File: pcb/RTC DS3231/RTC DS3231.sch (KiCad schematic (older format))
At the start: 19 parts, among them J101 Conn_01x06_Male, J102 Conn_01x04_Male, U101 DS3231M, U102 AT24CS32-SSHM

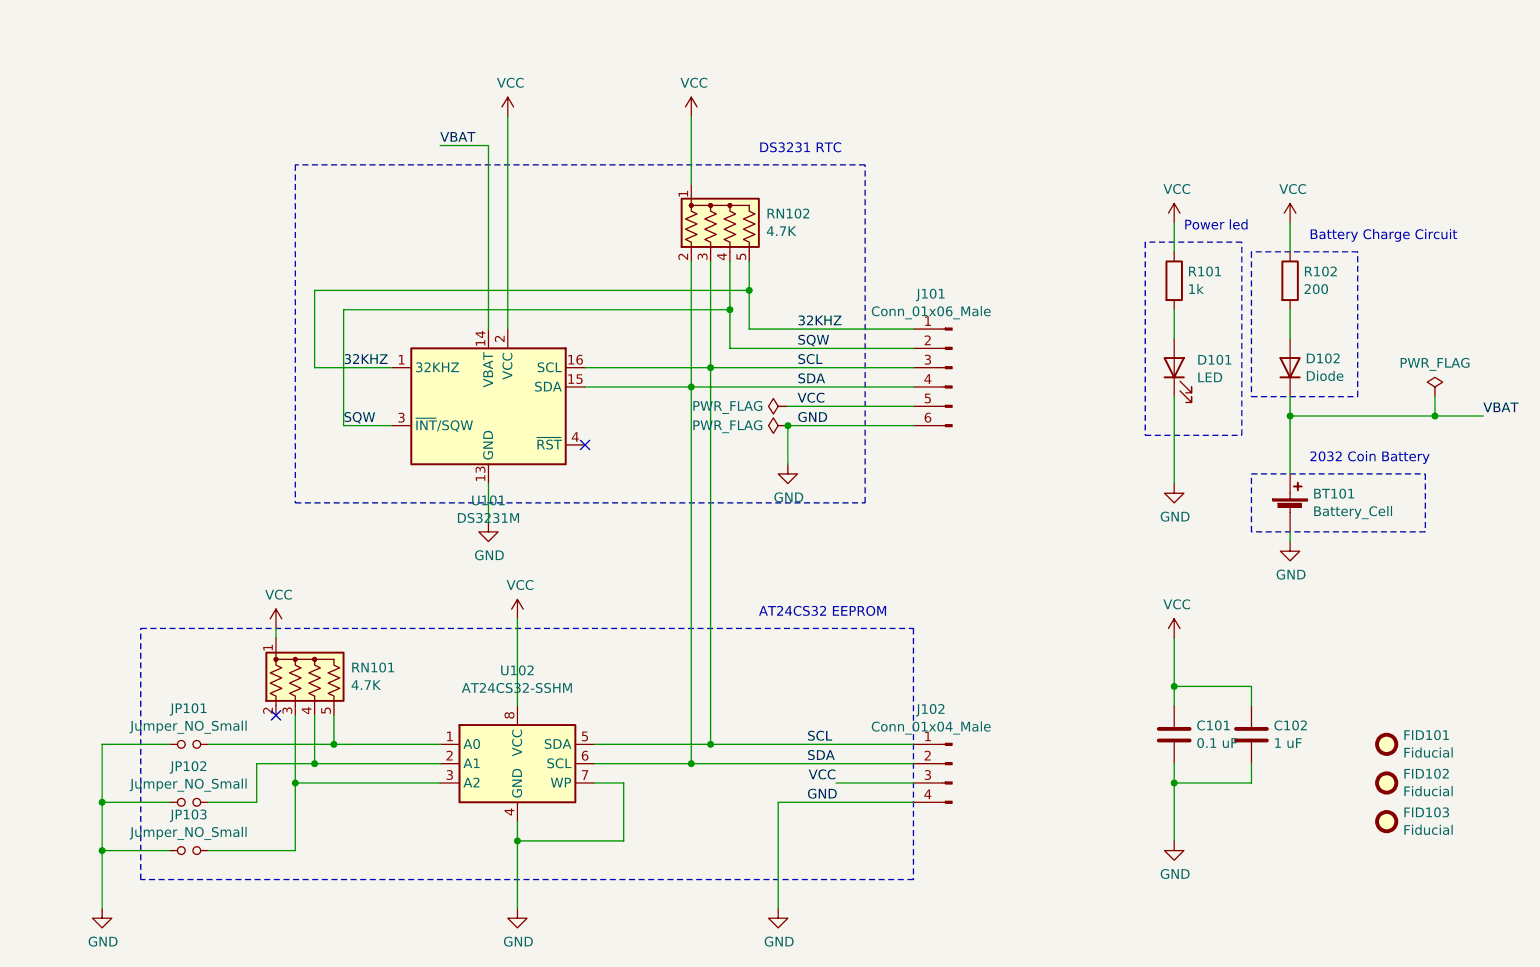
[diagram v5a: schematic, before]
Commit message: Update RTC DS3231.sch
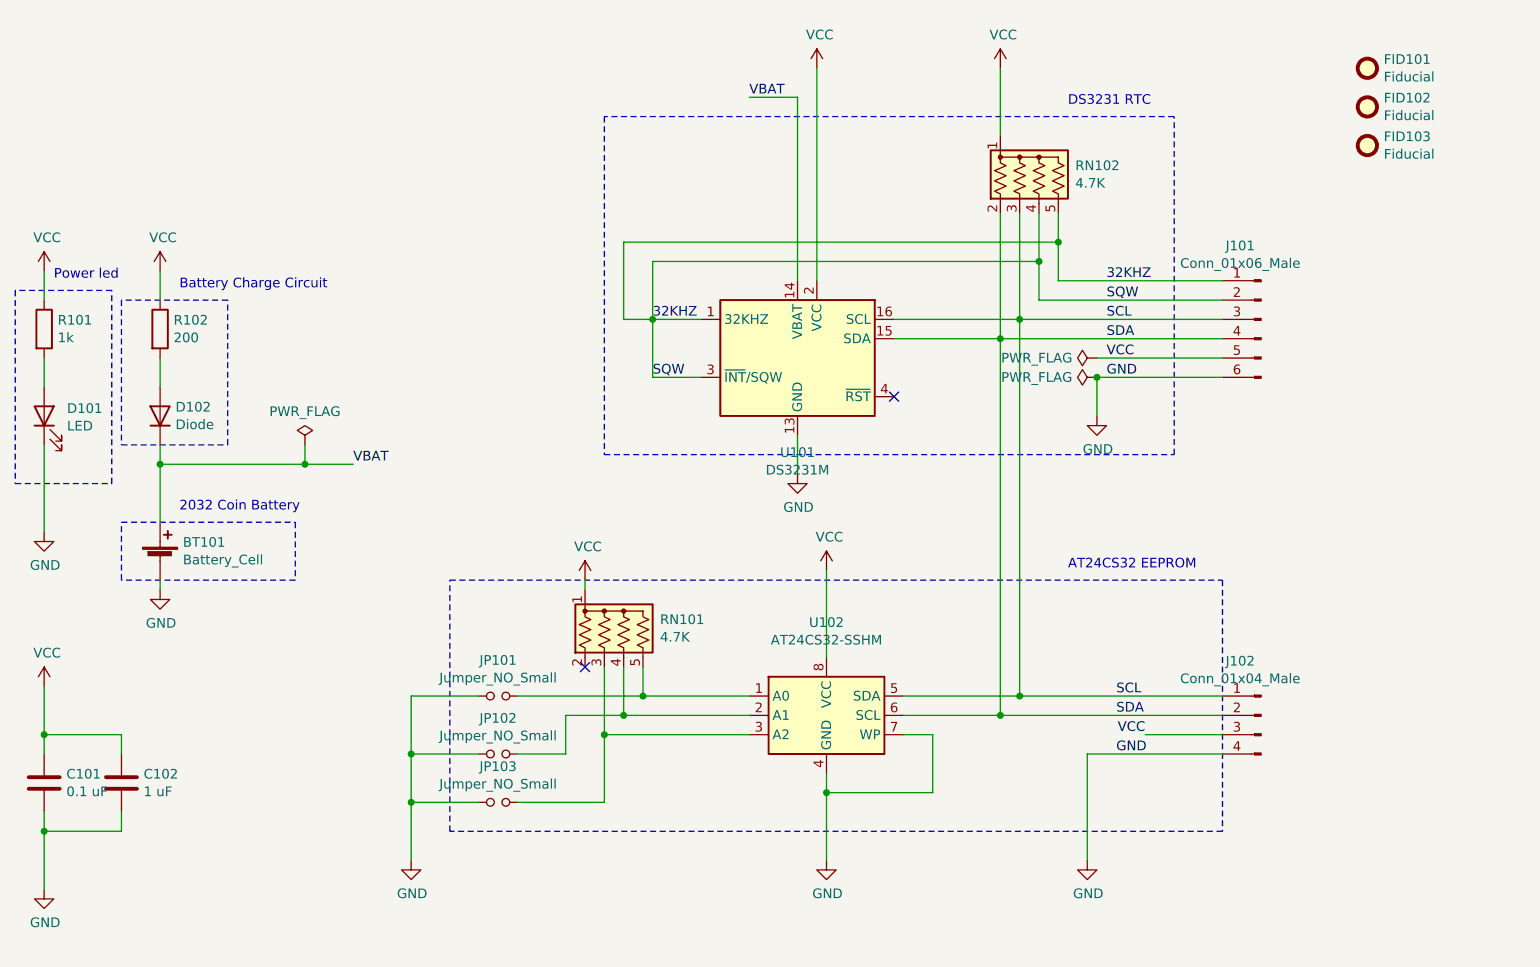
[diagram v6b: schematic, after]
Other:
- moved on the sheet: BT101, C101, C102, D101, D102, FID101, FID102, FID103, J101, J102, JP101, JP102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

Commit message: Updates schematic and footprints.
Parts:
- FID101, FID102, FID103: footprint (none) -> Fiducial:Fiducial_1.5mm_Mask3mm
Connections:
- net 32KHZ: no longer J101.2 (Pin_2), RN102.4 (R3), U101.3 (~INT~/SQW)
- new net SQW: J101.2 (Pin_2), RN102.4 (R3), U101.3 (~INT~/SQW)
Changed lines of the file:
@@
 SDA
-Wire Wire Line
-	8200 2200 8200 2350
 Wire Wire Line
 	8200 2550 9050 2550
@@
 	-1   0    0    -1
 $EndComp
-Text Label 6100 3050 0    50   ~ 0
-SQW
 Wire Wire Line
 	7400 4800 7900 4800
@@
 Wire Wire Line
 	6600 1600 6850 1600
-Wire Wire Line
-	6350 3050 6100 3050
 Wire Wire Line
 	8650 4900 9050 4900
@@
 F 0 "FID103" H 9885 1896 50  0000 L CNN
 F 1 "Fiducial" H 9885 1805 50  0000 L CNN
-F 2 "" H 9800 1850 50  0001 C CNN
+F 2 "Fiducial:Fiducial_1.5mm_Mask3mm" H 9800 1850 50  0001 C CNN
 F 3 "~" H 9800 1850 50  0001 C CNN
 	1    9800 1850
@@
 F 0 "FID102" H 9885 1696 50  0000 L CNN
 F 1 "Fiducial" H 9885 1605 50  0000 L CNN
-F 2 "" H 9800 1650 50  0001 C CNN
+F 2 "Fiducial:Fiducial_1.5mm_Mask3mm" H 9800 1650 50  0001 C CNN
 F 3 "~" H 9800 1650 50  0001 C CNN
 	1    9800 1650
@@
 F 0 "FID101" H 9885 1496 50  0000 L CNN
 F 1 "Fiducial" H 9885 1405 50  0000 L CNN
-F 2 "" H 9800 1450 50  0001 C CNN
+F 2 "Fiducial:Fiducial_1.5mm_Mask3mm" H 9800 1450 50  0001 C CNN
 F 3 "~" H 9800 1450 50  0001 C CNN
 	1    9800 1450
 	1    0    0    -1
 $EndComp
-Wire Wire Line
-	5950 2750 5950 2350
-Wire Wire Line
-	5950 2350 8200 2350
-Connection ~ 8200 2350
-Wire Wire Line
-	8200 2350 8200 2550
-Text Label 6100 2750 0    50   ~ 0
-32KHZ
-Wire Wire Line
-	8100 2200 8100 2450
-Wire Wire Line
-	6100 2450 8100 2450
-Connection ~ 8100 2450
-Wire Wire Line
-	8100 2450 8100 2650
-Wire Wire Line
-	5950 2750 6100 2750
-Wire Wire Line
-	6100 2450 6100 2750
 Text Label 8450 2950 0    50   ~ 0
 VCC
@@
 Wire Wire Line
 	4850 5000 4850 5250
-Connection ~ 6100 2750
 Wire Wire Line
 	6100 2750 6350 2750
 Wire Wire Line
-	6100 2750 6100 3050
+	6350 3050 6100 3050
+Text Label 6100 3050 0    50   ~ 0
+SQW
+Text Label 6100 2750 0    50   ~ 0
+32KHZ
+Wire Wire Line
+	8200 2200 8200 2550
+Wire Wire Line
+	8100 2200 8100 2650
 $EndSCHEMATC

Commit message: Mounting Holes added.
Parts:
- added H101, H102, H103: MountingHole, MountingHole:MountingHole_2.5mm_Pad_TopOnly, symbol Mechanical:MountingHole
- FID101, FID102, FID103: footprint Fiducial:Fiducial_1.5mm_Mask3mm -> Fiducial:Fiducial_0.5mm_Mask1mm
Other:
- note added: "Fiducials"
- note added: "Mounting Holes"
- moved on the sheet: FID101, FID102, FID103
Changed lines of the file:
@@
 L Mechanical:Fiducial FID103
 U 1 1 61580870
-P 9800 1850
-F 0 "FID103" H 9885 1896 50  0000 L CNN
-F 1 "Fiducial" H 9885 1805 50  0000 L CNN
-F 2 "Fiducial:Fiducial_1.5mm_Mask3mm" H 9800 1850 50  0001 C CNN
-F 3 "~" H 9800 1850 50  0001 C CNN
-	1    9800 1850
+P 2950 1950
+F 0 "FID103" H 3035 1996 50  0000 L CNN
+F 1 "Fiducial" H 3035 1905 50  0000 L CNN
+F 2 "Fiducial:Fiducial_0.5mm_Mask1mm" H 2950 1950 50  0001 C CNN
+F 3 "~" H 2950 1950 50  0001 C CNN
+	1    2950 1950
 	1    0    0    -1
 $EndComp
@@
 L Mechanical:Fiducial FID102
 U 1 1 61580E6C
-P 9800 1650
-F 0 "FID102" H 9885 1696 50  0000 L CNN
-F 1 "Fiducial" H 9885 1605 50  0000 L CNN
-F 2 "Fiducial:Fiducial_1.5mm_Mask3mm" H 9800 1650 50  0001 C CNN
-F 3 "~" H 9800 1650 50  0001 C CNN
-	1    9800 1650
+P 2950 1750
+F 0 "FID102" H 3035 1796 50  0000 L CNN
+F 1 "Fiducial" H 3035 1705 50  0000 L CNN
+F 2 "Fiducial:Fiducial_0.5mm_Mask1mm" H 2950 1750 50  0001 C CNN
+F 3 "~" H 2950 1750 50  0001 C CNN
+	1    2950 1750
 	1    0    0    -1
 $EndComp
@@
 L Mechanical:Fiducial FID101
 U 1 1 615818A5
-P 9800 1450
-F 0 "FID101" H 9885 1496 50  0000 L CNN
-F 1 "Fiducial" H 9885 1405 50  0000 L CNN
-F 2 "Fiducial:Fiducial_1.5mm_Mask3mm" H 9800 1450 50  0001 C CNN
-F 3 "~" H 9800 1450 50  0001 C CNN
-	1    9800 1450
+P 2950 1550
+F 0 "FID101" H 3035 1596 50  0000 L CNN
+F 1 "Fiducial" H 3035 1505 50  0000 L CNN
+F 2 "Fiducial:Fiducial_0.5mm_Mask1mm" H 2950 1550 50  0001 C CNN
+F 3 "~" H 2950 1550 50  0001 C CNN
+	1    2950 1550
 	1    0    0    -1
 $EndComp
@@
 Wire Wire Line
 	8100 2200 8100 2650
+Wire Notes Line
+	3450 2050 3450 1400
+Wire Notes Line
+	3450 1400 2850 1400
+Wire Notes Line
+	2850 1400 2850 2050
+Wire Notes Line
+	2850 2050 3450 2050
+$Comp
+L Mechanical:MountingHole H101
+U 1 1 615F5205
+P 3800 1500
+F 0 "H101" H 3900 1546 50  0000 L CNN
+F 1 "MountingHole" H 3900 1455 50  0000 L CNN
+F 2 "MountingHole:MountingHole_2.5mm_Pad_TopOnly" H 3800 1500 50  0001 C CNN
+F 3 "~" H 3800 1500 50  0001 C CNN
+	1    3800 1500
+	1    0    0    -1
+$EndComp
+$Comp
+L Mechanical:MountingHole H102
+U 1 1 615F579C
+P 3800 1700
+F 0 "H102" H 3900 1746 50  0000 L CNN
+F 1 "MountingHole" H 3900 1655 50  0000 L CNN
+F 2 "MountingHole:MountingHole_2.5mm_Pad_TopOnly" H 3800 1700 50  0001 C CNN
+F 3 "~" H 3800 1700 50  0001 C CNN
+	1    3800 1700
+	1    0    0    -1
+$EndComp
+$Comp
+L Mechanical:MountingHole H103
+U 1 1 615F5958
+P 3800 1950
+F 0 "H103" H 3900 1996 50  0000 L CNN
+F 1 "MountingHole" H 3900 1905 50  0000 L CNN
+F 2 "MountingHole:MountingHole_2.5mm_Pad_TopOnly" H 3800 1950 50  0001 C CNN
+F 3 "~" H 3800 1950 50  0001 C CNN
+	1    3800 1950
+	1    0    0    -1
+$EndComp
+Wire Notes Line
+	3650 1350 4500 1350
+Wire Notes Line
+	4500 1350 4500 2100
+Wire Notes Line
+	4500 2100 3650 2100
+Wire Notes Line
+	3650 2100 3650 1350
+Text Notes 2850 1350 0    50   ~ 0
+Fiducials
+Text Notes 3650 1300 0    50   ~ 0
+Mounting Holes
 $EndSCHEMATC
